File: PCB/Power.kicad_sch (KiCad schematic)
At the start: 8 parts, among them IC5 TLV75533PDBVR, J1 XT90PW_M

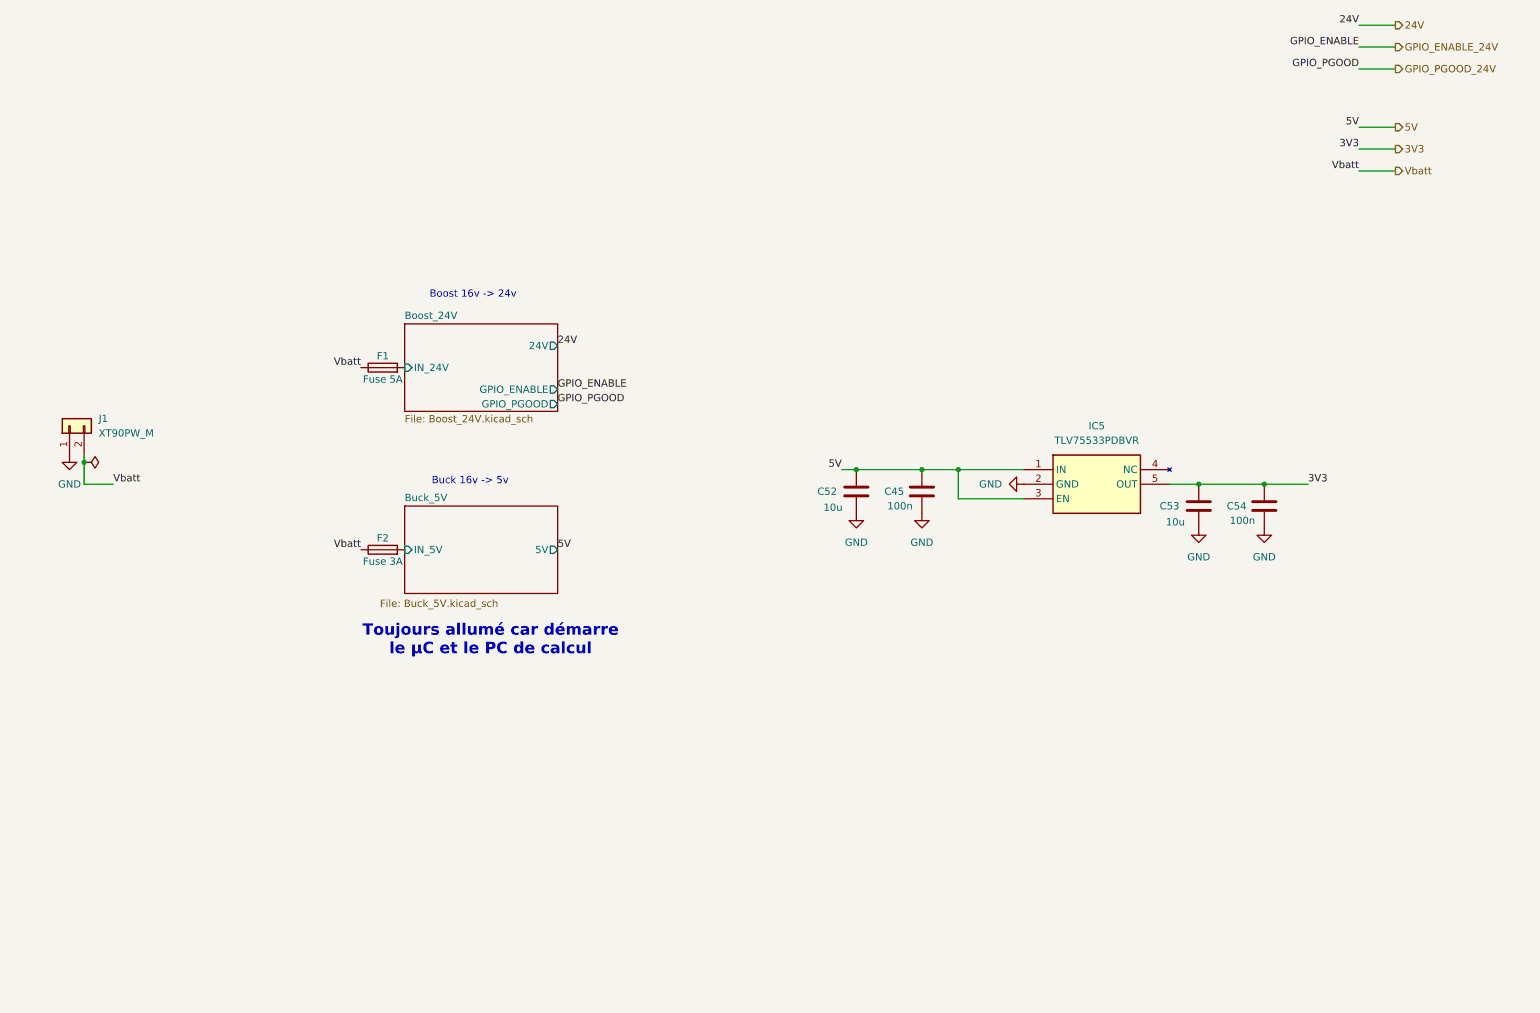
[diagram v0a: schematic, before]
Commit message: Updated a lot of stuff:
Added encoders,
Added 5V power supply for actuators
Added 12V power supply for actuators
Renamed sheets to be clearer
Added usb debug
Modify MCU sheet to be A3 format
Linked some pins
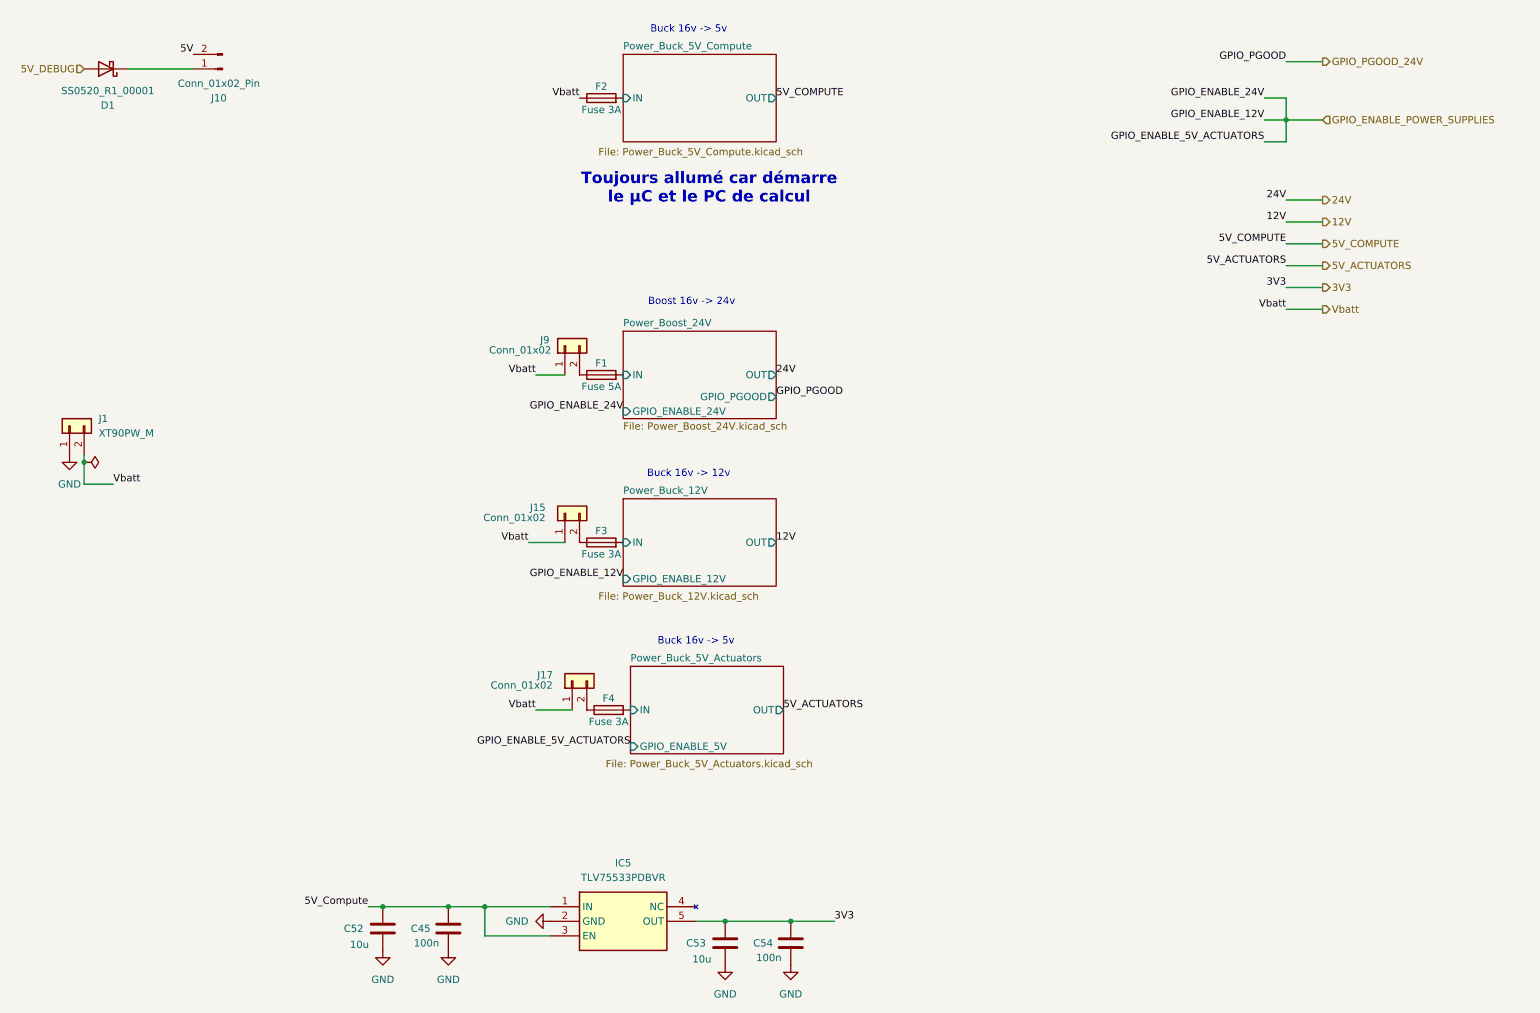
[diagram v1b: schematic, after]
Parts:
- added D1: SS0520_R1_00001, symbol Device:D_Schottky
- added F3, F4: Fuse 3A, symbol Device:Fuse
- added J10: Conn_01x02_Pin, symbol Connector:Conn_01x02_Pin
- added J15, J17, J9: Conn_01x02, Connector_PinHeader_2.54mm:PinHeader_1x02_P2.54mm_Vertical, symbol Connector_Generic:Conn_01x02
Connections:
- net 5V: now also J10.2 (Pin_2); no longer C45.1, C52.1, IC5.1 (IN), IC5.3 (EN)
- net Vbatt: now also J15.1 (Pin_1), J17.1 (Pin_1), J9.1 (Pin_1); no longer F1.1
- net Power_Boost_24V/IN_24V renamed Power_Boost_24V/IN
- net Power_Buck_5V_Compute/IN_5V renamed Power_Buck_5V_Compute/IN
- new net: F4.1, J17.2 (Pin_2)
- new net: D1.1 (K), J10.1 (Pin_1)
- new net: F1.1, J9.2 (Pin_2)
- new net: F3.1, J15.2 (Pin_2)
- new net 5V_Compute: C45.1, C52.1, IC5.1 (IN), IC5.3 (EN)
- new net 5V_DEBUG: D1.2 (A)
- new net Power_Buck_12V/IN: F3.2
- new net Power_Buck_5V_Actuators/IN: F4.2
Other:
- sheet Boost_24V renamed Power_Boost_24V
- sheet Buck_5V renamed Power_Buck_5V_Compute
- added sheet Power_Buck_12V (Power_Buck_12V.kicad_sch)
- added sheet Power_Buck_5V_Actuators (Power_Buck_5V_Actuators.kicad_sch)
- sheet Power_Boost_24V: file Boost_24V.kicad_sch -> Power_Boost_24V.kicad_sch
- sheet Power_Boost_24V ports: added GPIO_ENABLE_24V, IN, OUT; removed 24V, GPIO_ENABLE, IN_24V
- sheet Power_Buck_5V_Compute: file Buck_5V.kicad_sch -> Power_Buck_5V_Compute.kicad_sch
- sheet Power_Buck_5V_Compute ports: added IN, OUT; removed 5V, IN_5V
- note added: "Buck 16v -> 12v"
- moved on the sheet: C45, C52, C53, C54, F1, F2, IC5
